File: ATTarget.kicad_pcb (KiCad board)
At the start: 2 copper layers, 28.2 x 50.8 mm, 20 parts, among them J1 ICSP, J2 Status, J3 FTDI, SW1 Power, U1 ATtiny85-20PU, U2 ATmega328-PU, Y1 16MHz

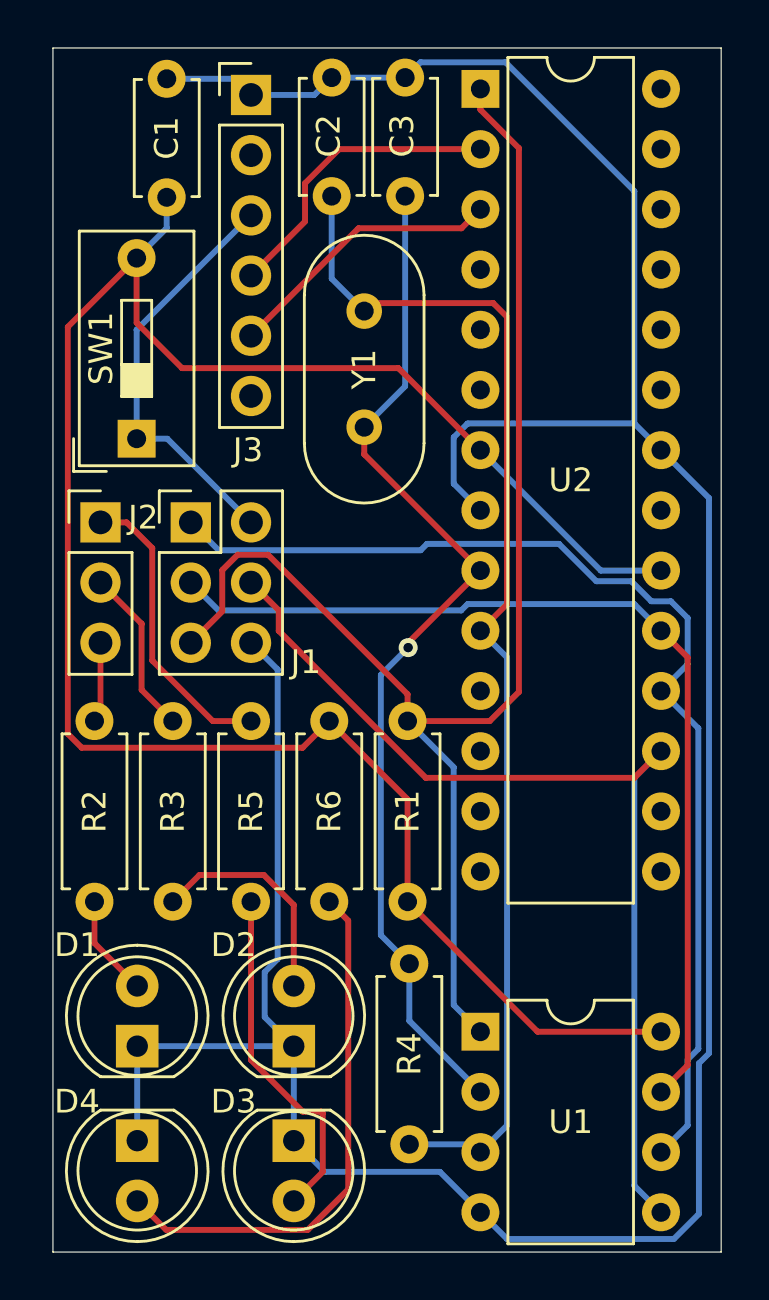
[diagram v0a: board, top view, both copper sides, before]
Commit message: Move C1 closer to where it's needed.
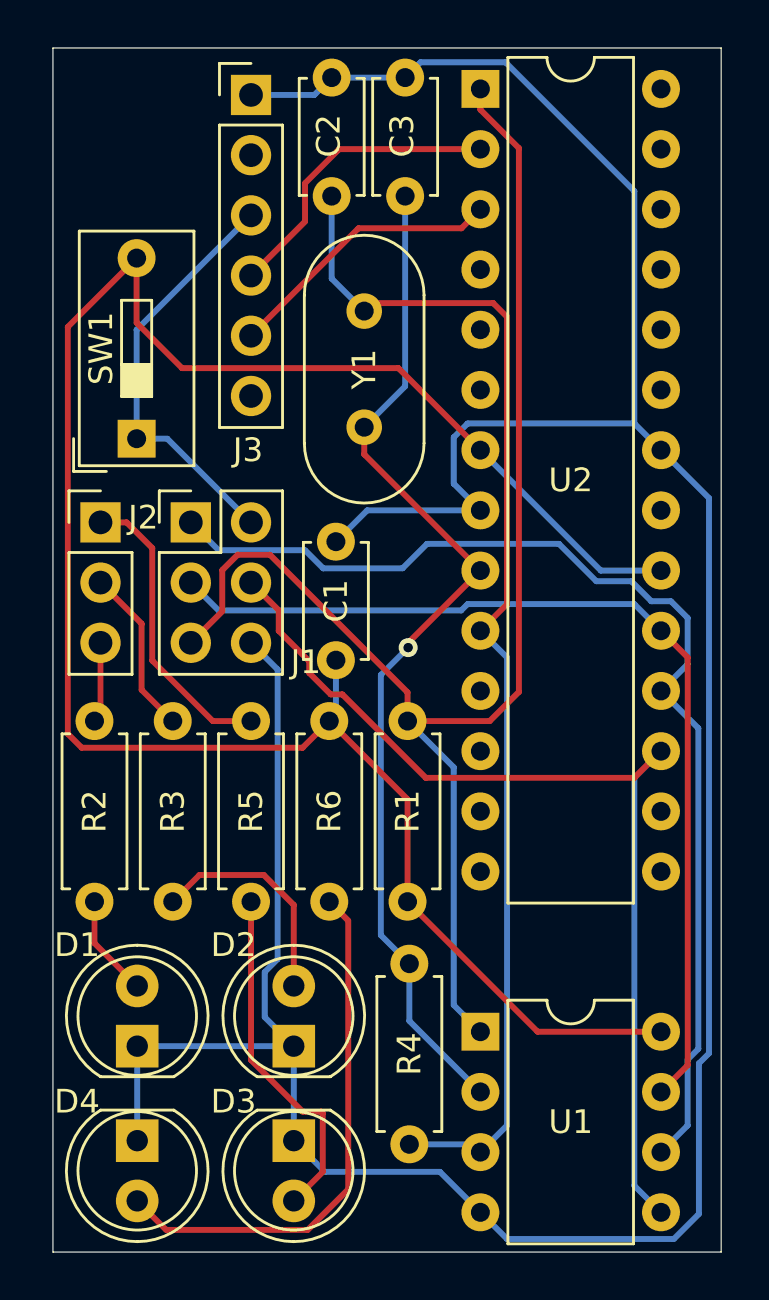
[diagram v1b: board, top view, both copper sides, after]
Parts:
- moved C1 20.8 mm to (111.5, 89.3)
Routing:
- net GND: track 130.9 -> 134.7 mm
- net /MISO: track 47.2 -> 47.8 mm

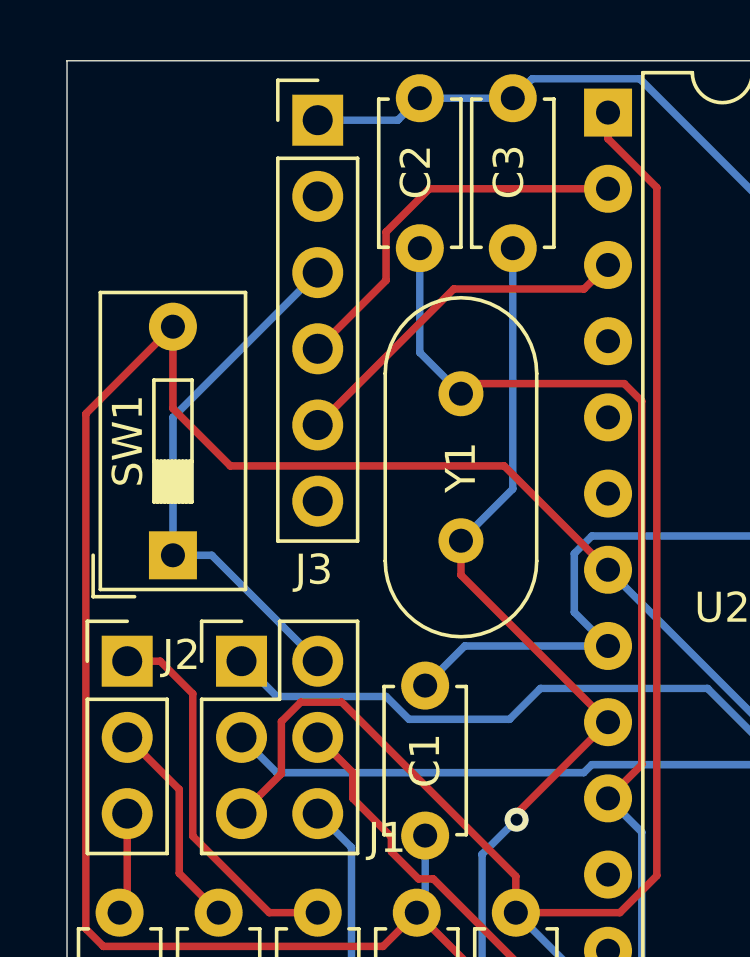
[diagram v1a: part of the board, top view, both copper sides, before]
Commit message: Fix FTDI.
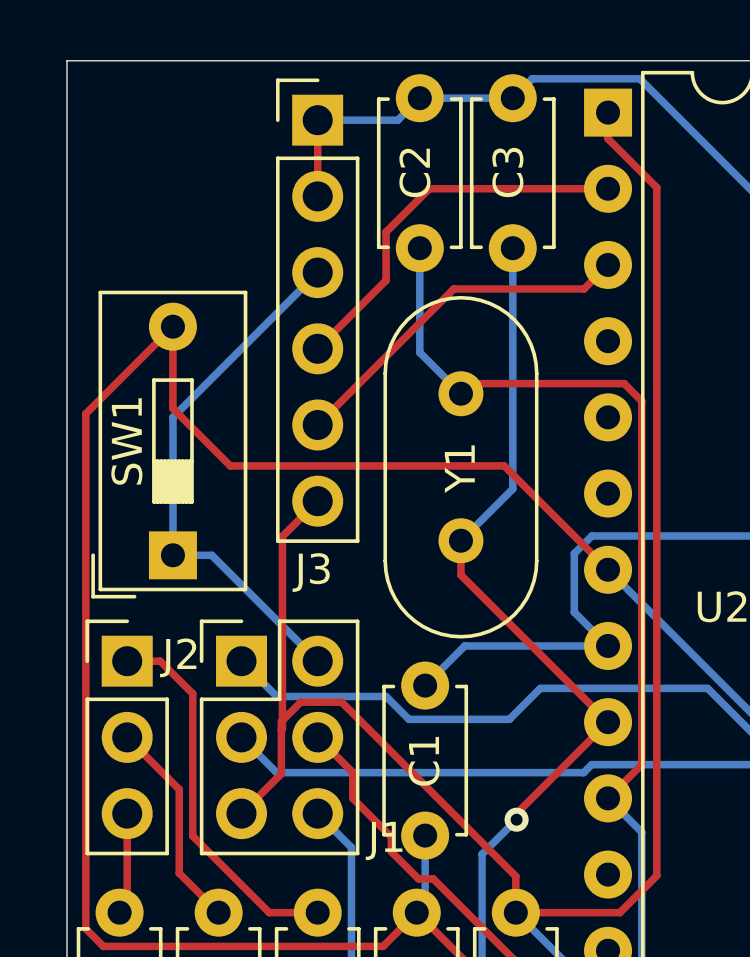
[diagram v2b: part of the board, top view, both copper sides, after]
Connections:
- J3 pad 2: Net-(J3-Pad2) -> GND
- J3 pad 6: Net-(J3-Pad6) -> /Reset
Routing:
- net /Reset: track 61.0 -> 69.2 mm
- net GND: track 134.7 -> 137.2 mm

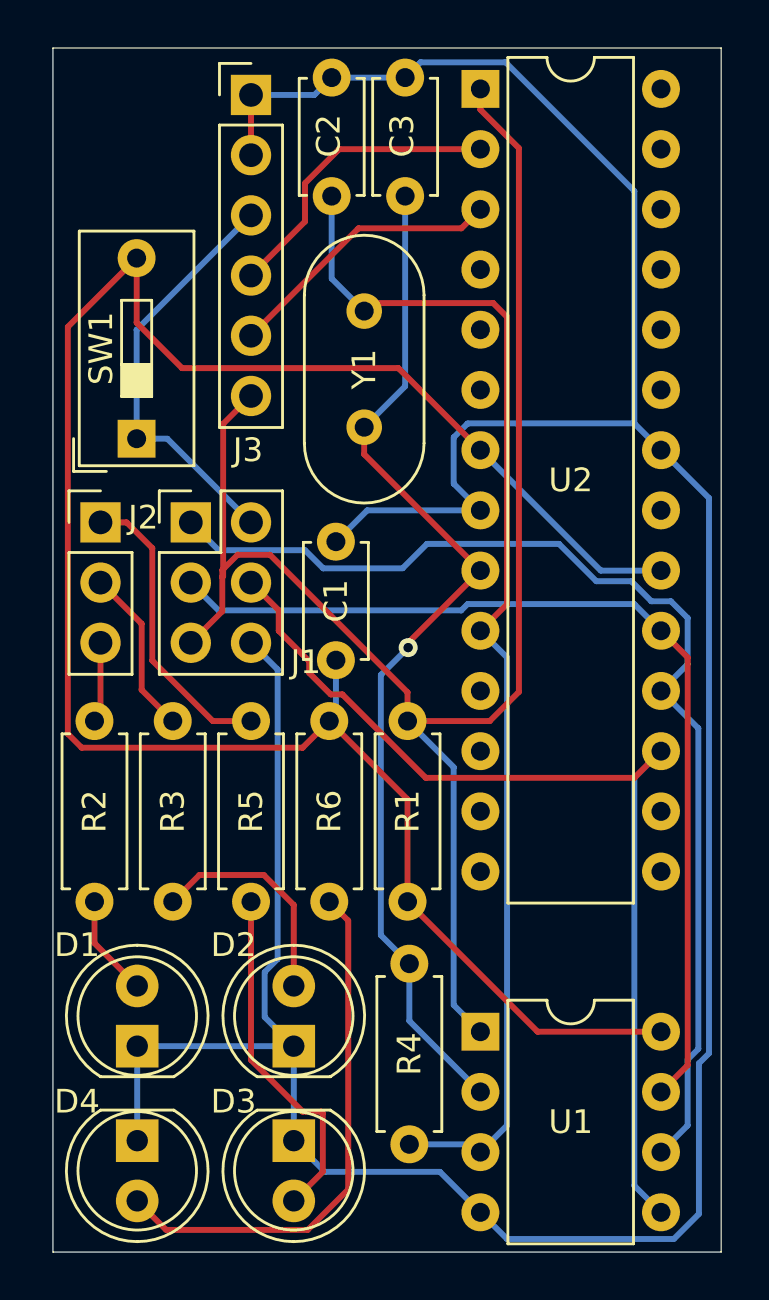
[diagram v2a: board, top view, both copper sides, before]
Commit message: Put a capacitor in between DTR and reset.
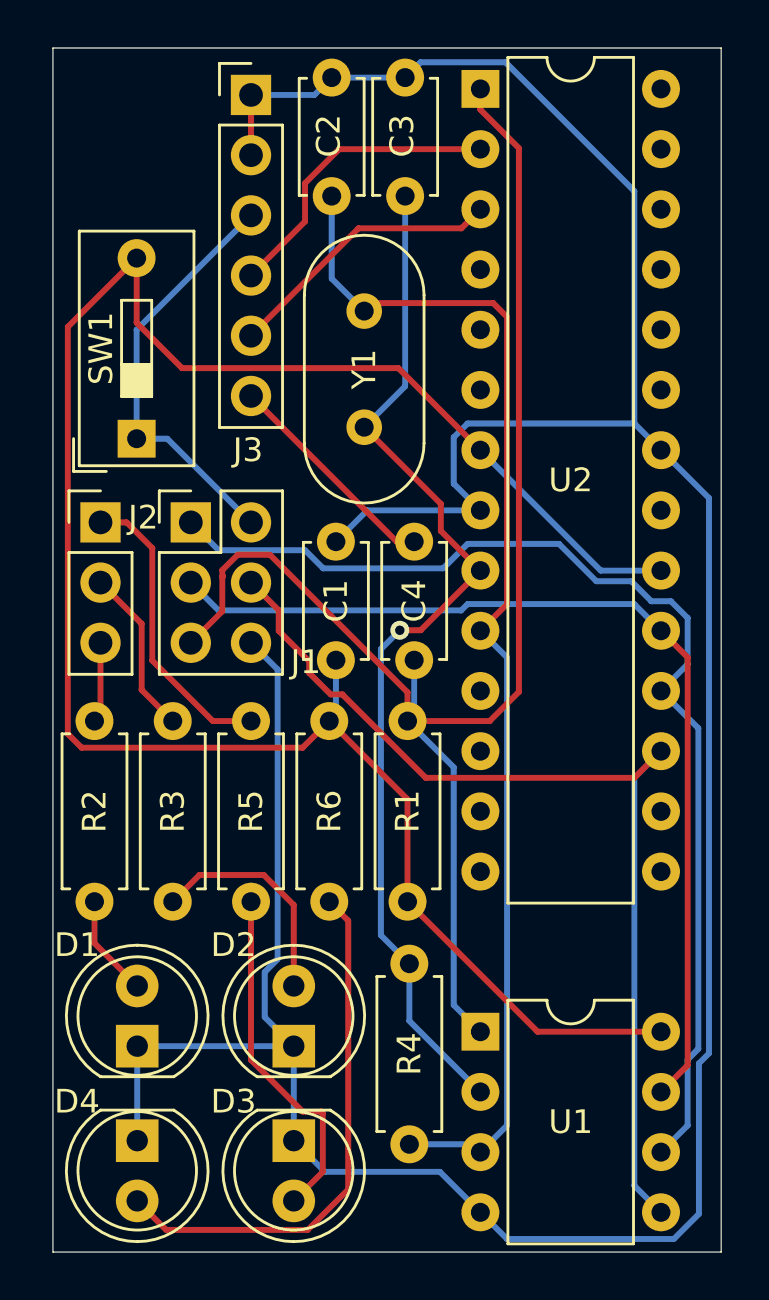
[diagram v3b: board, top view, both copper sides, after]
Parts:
- added C4: 100nF, Capacitor_THT:C_Disc_D4.7mm_W2.5mm_P5.00mm, F.Cu at (114.8, 84.3)
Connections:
- J3 pad 6: /Reset -> Net-(C4-Pad1)
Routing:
- net Net-(C4-Pad1): track 0.00 -> 9.43 mm
- net /Reset: track 69.2 -> 63.8 mm
- net /XTAL1: track 44.0 -> 44.5 mm
